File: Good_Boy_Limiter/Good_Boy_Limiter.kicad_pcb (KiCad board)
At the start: 2 copper layers, 107 parts, among them CN1 XT30PW-M, CN2 XT30PW-M, J1 UART, J2 Extra General Pins, Q1 STB15810, Q2 AO3422, Q4 AO3400A, SW3 RESET1, SW4 BOOT1, U1 ESP32-S3-WROOM-1, U10 B3B-XH-A, U11 B3B-XH-A, U12 B3B-XH-A, U3 LM5069MM-2/NOPB, U4 USBLC6-2SC6, U5 SY8120B, U6 1-178136-3, U7 LM5013DDAR, U8 B3B-XH-A

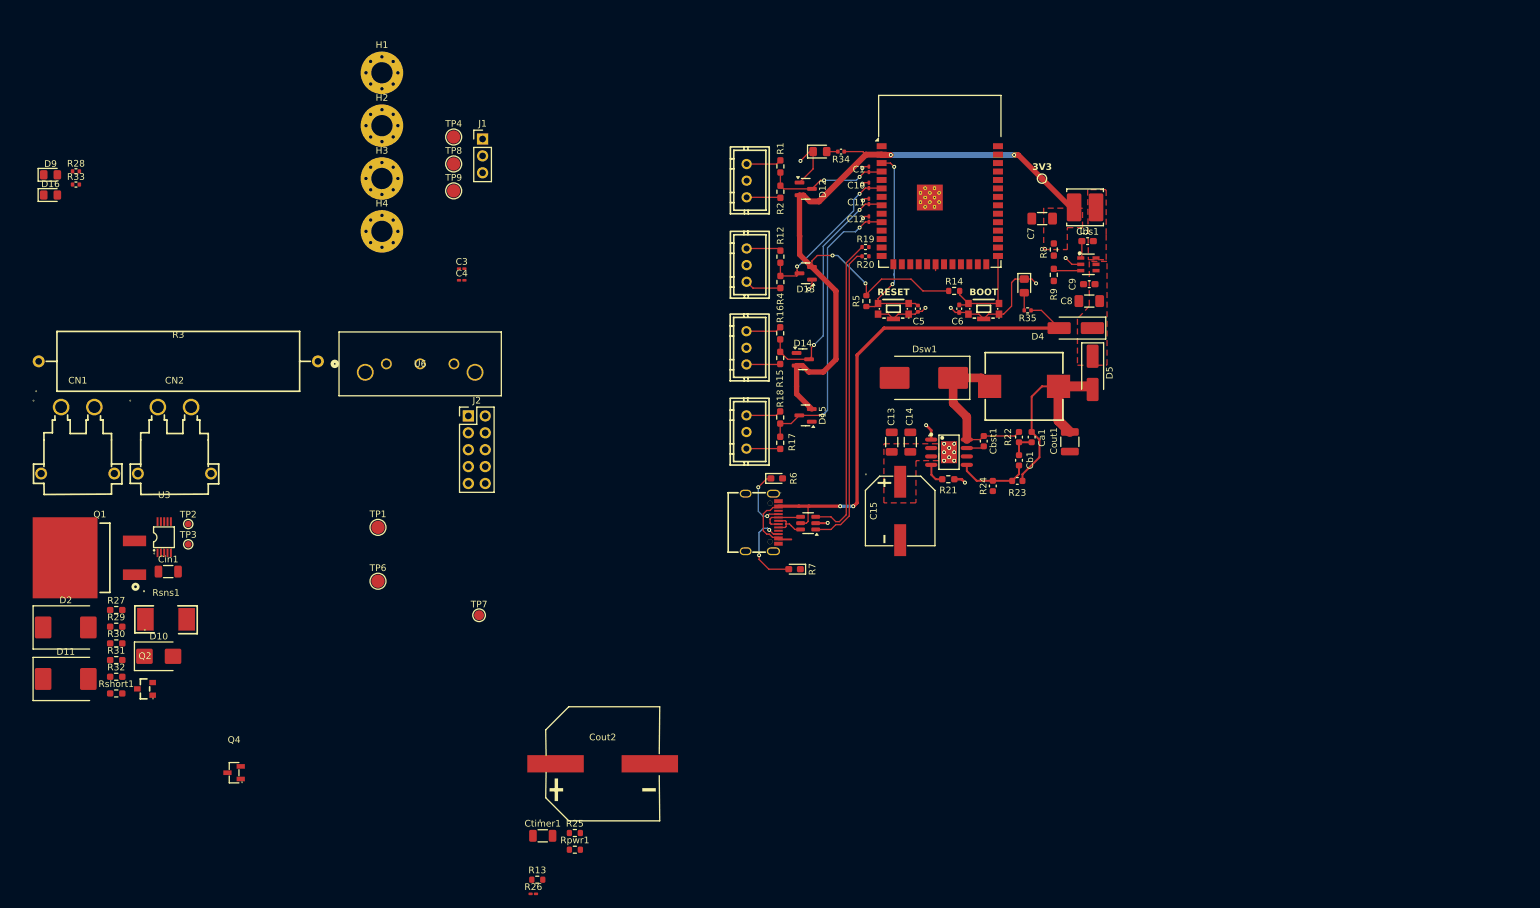
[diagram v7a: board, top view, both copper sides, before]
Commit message: Updated routing
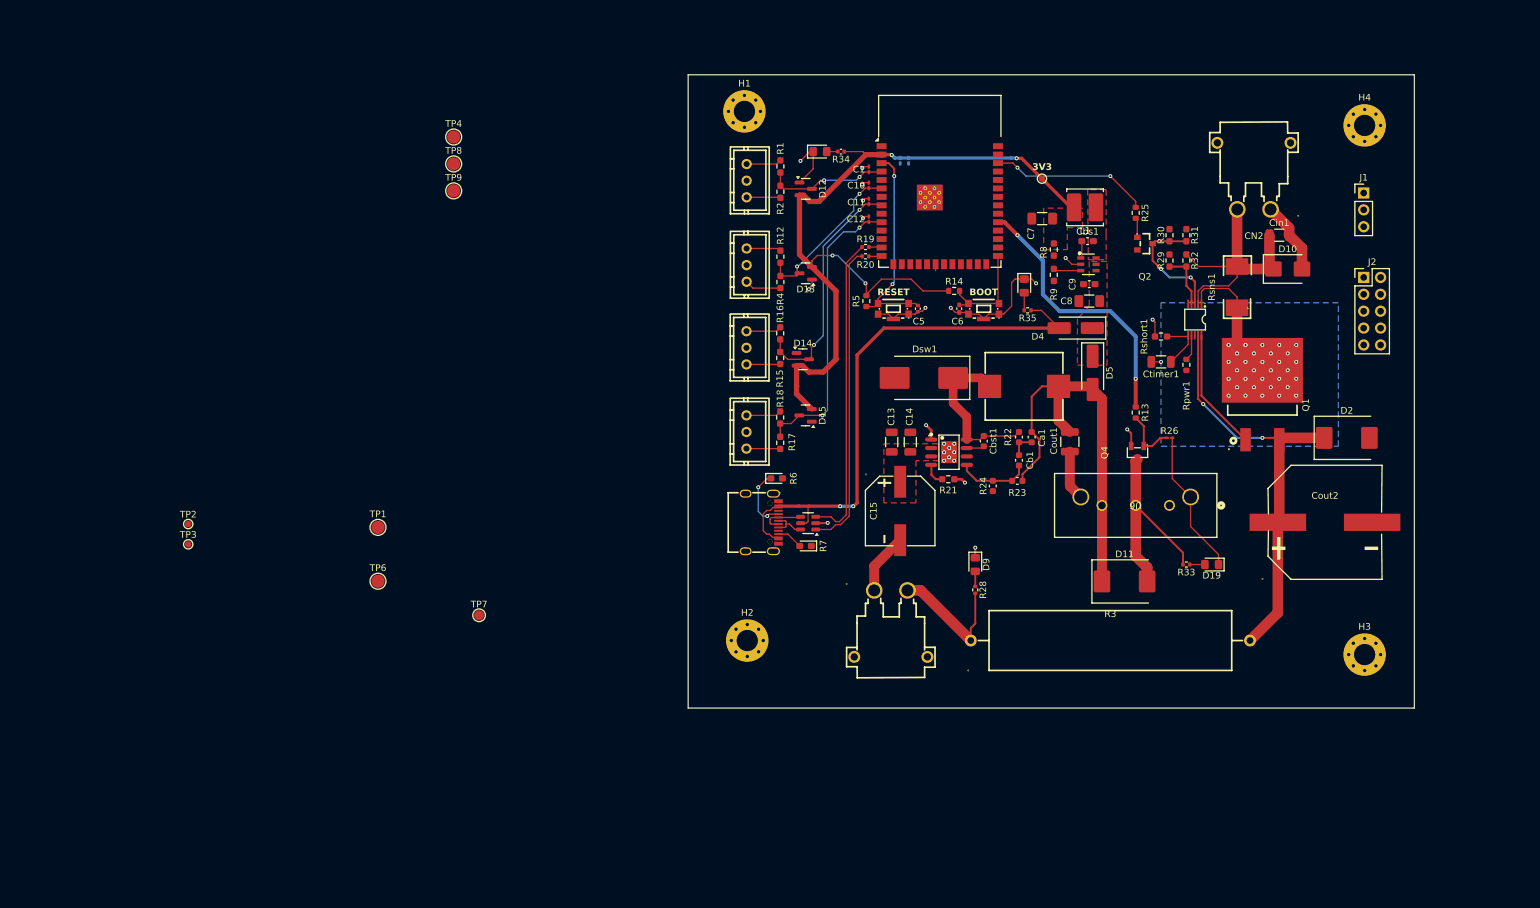
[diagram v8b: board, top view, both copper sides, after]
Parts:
- removed D16: LED, LED_SMD:LED_0805_2012Metric_Pad1.15x1.40mm_HandSolder
- removed R27: 10k, Resistor_SMD:R_0603_1608Metric_Pad0.98x0.95mm_HandSolder
- added D19: LED, LED_SMD:LED_0805_2012Metric_Pad1.15x1.40mm_HandSolder, F.Cu at (201.9, 102.9)
- C3, C4: moved to B.Cu
- moved D2 194.8 mm to (222.2, 83.8)
- moved D10 179.5 mm to (213.4, 58.4)
- moved R33 176.5 mm to (198.1, 102.9), turned to 180 degrees
- moved Q1 176.4 mm to (209.6, 78.9), turned to -90 degrees
- moved Cin1 174.6 mm to (212.1, 53.3)
- moved R31 173.2 mm to (198.1, 53.3), turned to -90 degrees
- moved R32 172.7 mm to (198.1, 57.1), turned to -90 degrees
- moved R30 169.9 mm to (195.6, 53.3), turned to 90 degrees
- moved Rsns1 168.6 mm to (205.7, 61.1), turned to 90 degrees
- moved R29 167.7 mm to (195.6, 57.1), turned to 90 degrees
- moved CN2 167.1 mm to (208.3, 44.5), turned to 180 degrees
- moved Rshort1 166.1 mm to (194.3, 68.6), turned to 180 degrees
- moved Q2 164.6 mm to (191.9, 54.6), turned to 180 degrees
- moved H3 164.2 mm to (224.9, 116.4)
- moved D11 159.9 mm to (188.8, 105.4)
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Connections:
- net Net-(Q1-D) renamed /In-rush controller/Power_Drain
- R13 pad 1: /GPIO6 -> /GPIO38
- R25 pad 1: /In-rush controller/GPIO6 -> /GPIO2
- R33 pad 1: GND -> Net-(D19-A)
- R33 pad 2: Net-(D16-A) -> Net-(D11-A)
- U3 pad 8: Net-(U3-PGD) -> unconnected-(U3-PGD-Pad8)
- U6 pad 4: (no net) -> GND
- U6 pad 5: (no net) -> GND
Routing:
- net /In-rush controller/+48VOUT: track 0.00 -> 63.2 mm, vias 0 -> 2
- net GND: track 70.3 -> 128.2 mm, vias 21 -> 25
- net /GPIO38: track 0.00 -> 41.4 mm, vias 0 -> 2
- net +48VIN: track 0.00 -> 39.0 mm
- net Net-(D11-A): track 0.00 -> 31.4 mm
- net /+12V: track 31.8 -> 61.2 mm
- net /GPIO2: track 0.00 -> 24.0 mm, vias 0 -> 2
- net /In-rush controller/Power_Drain: track 0.00 -> 20.6 mm, vias 0 -> 32
- net +48VOUT: track 0.00 -> 20.0 mm
- net Net-(Q2-D): track 0.00 -> 18.8 mm, vias 0 -> 2
- net Net-(Q1-G): track 0.00 -> 18.5 mm
- net Net-(USB1-CC2): track 12.7 -> 3.94 mm, vias 2 -> 0
- net Net-(Q4-G): track 0.00 -> 8.67 mm
- net Net-(U3-OVLO): track 0.00 -> 8.49 mm
- net Net-(U3-TIMER): track 0.00 -> 8.33 mm
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- added copper zone on B.Cu, net /In-rush controller/Power_Drain
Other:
- board outline added: 109.2 x 95.2 mm
